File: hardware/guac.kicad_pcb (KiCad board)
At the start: 4 copper layers, 59.5 x 58.5 mm, 72 parts, among them J1 VBUS input fly-leads, J2 Orange TinySLED, J3 Orange TinySLED, J4 AM32 dual ESC, Q1 AO3402, U1 Seeed XIAO RP2350, U10 SK9822-EC20, U11 SN74HC595PWR, U12 SK9822-EC20, U2 AP63205WU-7, U4 LSM6DSV320XTR, U5 H3LIS331DLTR, U6 H3LIS331DLTR, U7 BetaFPV ELRS Lite, U8 SN74AHCT1G125, U9 SN74AHCT1G125

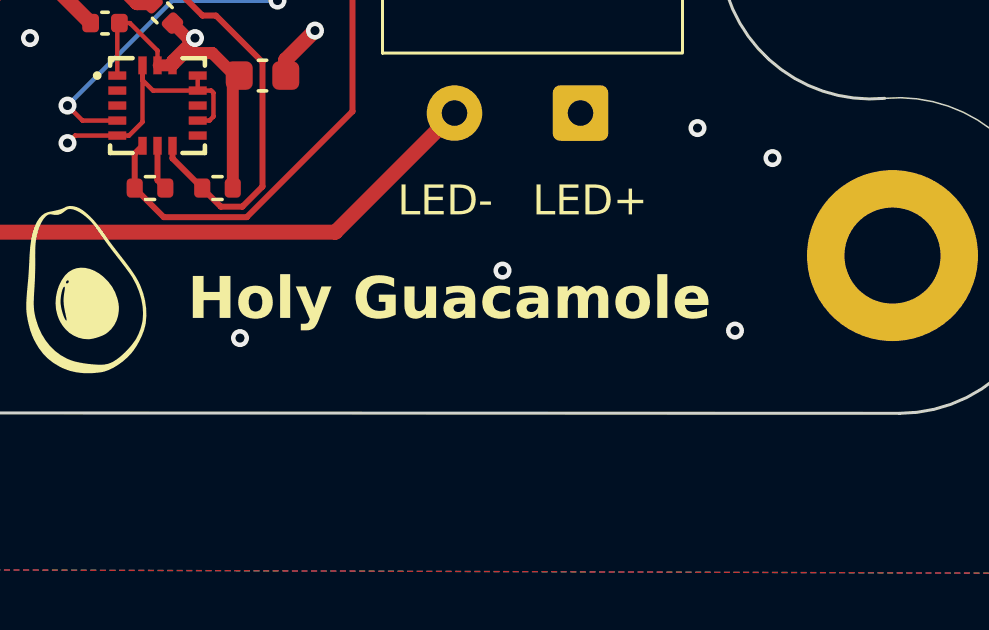
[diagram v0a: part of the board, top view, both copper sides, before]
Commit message: feat: update cad image and silkscreen
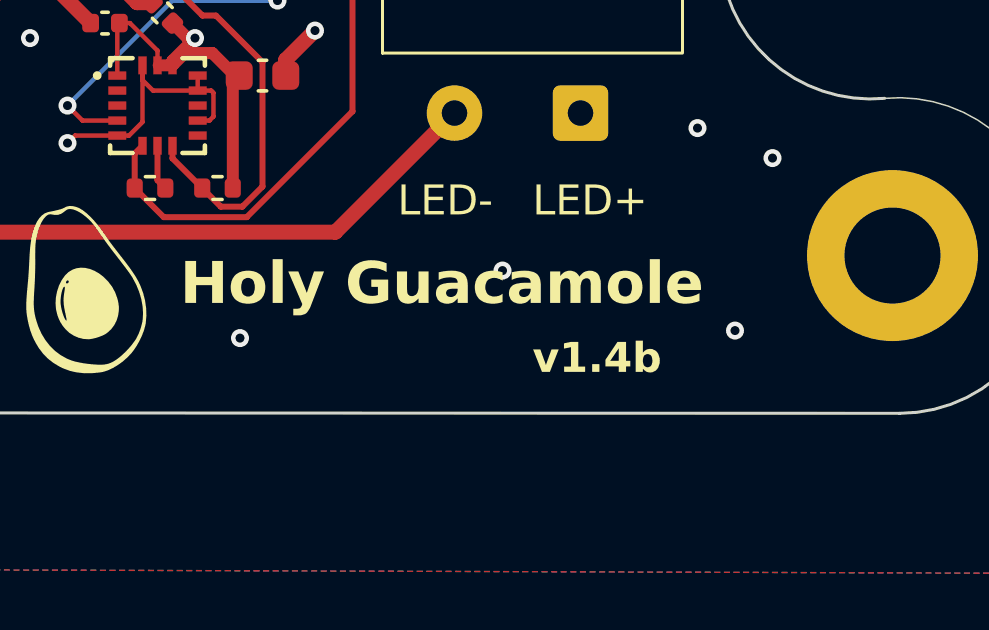
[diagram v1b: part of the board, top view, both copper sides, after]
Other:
- board text added: "v1.4b"
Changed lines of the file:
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@@
 	)
 	(paper "A4")
+	(title_block
+		(title "Holy Guacamole")
+		(date "2026-07-12")
+		(rev "1.4b")
+		(company "Kieran Klukas")
+	)
 	(layers
 		(0 "F.Cu" signal)
@@
 		)
 	)
+	(gr_text "v1.4b"
+		(at 116.25 130.25 0)
+		(layer "F.SilkS")
+		(effects
+			(font
+				(size 1 1)
+				(thickness 0.25)
+				(bold yes)
+			)
+			(justify left bottom)
+		)
+	)
 	(gr_text "Holy Guacamole"
-		(at 104.75 128.5 0)
+		(at 104.5 128 0)
 		(layer "F.SilkS")
 		(effects
@@
 		)
 	)
-	(barcode
-		(at 112.927175 116.177175 0)
-		(layer "B.SilkS")
-		(size 15.85435 15.85435)
-		(text "https://dunkirk.sh")
-		(text_height 1)
-		(type qr)
-		(ecc_level L)
-		(hide yes)
-		(knockout no)
-	)
 	(segment

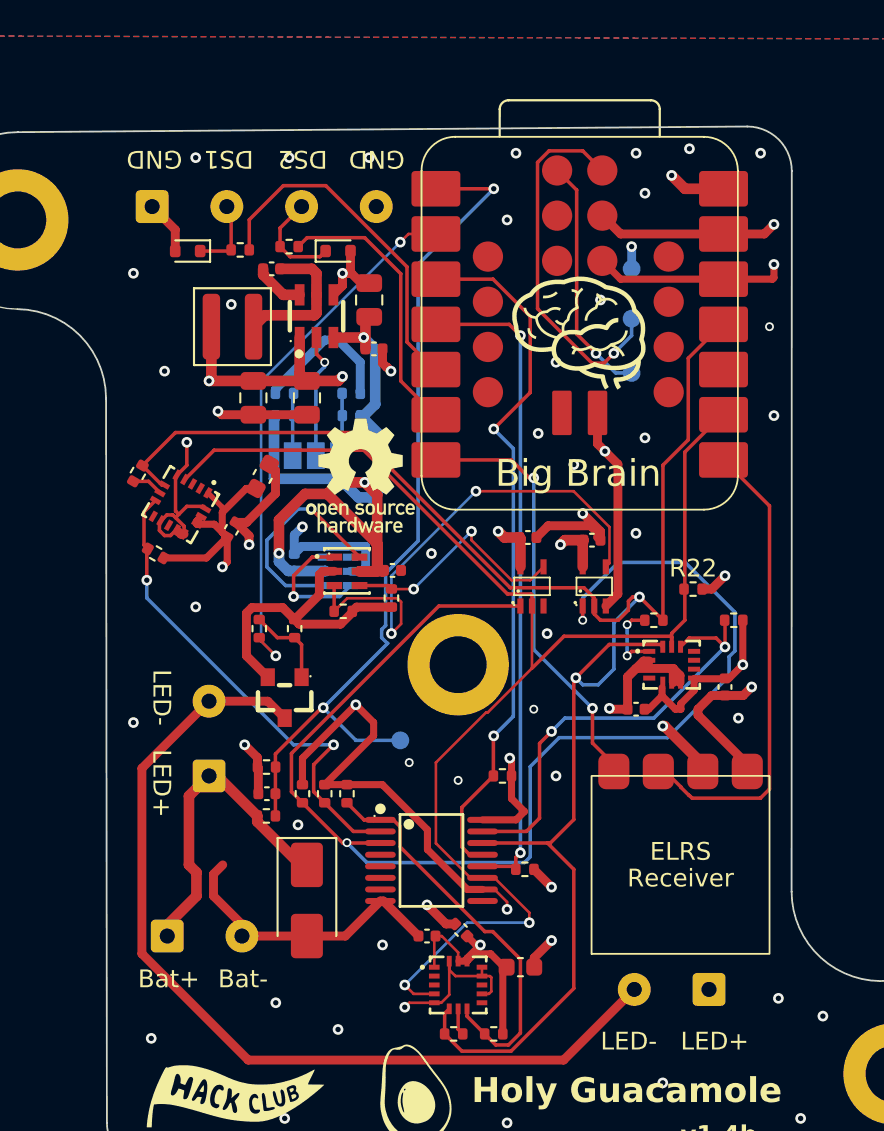
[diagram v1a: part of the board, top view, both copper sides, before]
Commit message: feat: update pcb to use new components
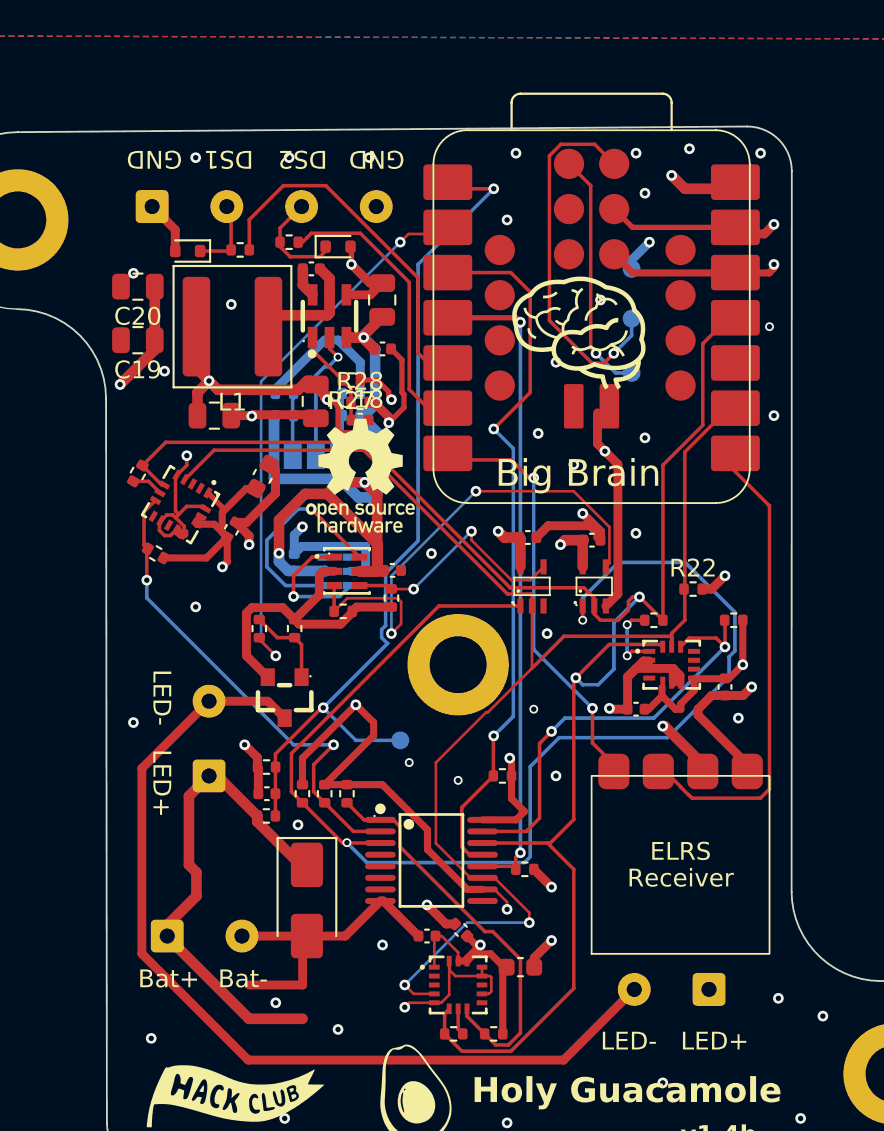
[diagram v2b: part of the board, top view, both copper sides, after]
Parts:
- added C18: 47pf, Capacitor_SMD:C_0402_1005Metric, F.Cu at (98.2, 89.5)
- added C19: 22uf, Capacitor_SMD:C_0805_2012Metric, F.Cu at (85.8, 85.0)
- added C20: 22uf, Capacitor_SMD:C_0805_2012Metric, F.Cu at (85.8, 82.0)
- added R27: 158kΩ, Resistor_SMD:R_0402_1005Metric, F.Cu at (97.8, 87.2)
- added R28: 30.1kΩ, Resistor_SMD:R_0402_1005Metric, F.Cu at (98.2, 88.5)
- L1: value 4.7uH -> 5.6uH; footprint Inductor_SMD:L_Wuerth_MAPI-4020 -> Inductor_SMD:L_Bourns_SRP6060FA
- U2: value AP63205WU-7 -> AP63300WU-7
- moved C5 2.41 mm to (90.0, 89.2), turned to 0 degrees
- moved C3 2.23 mm to (95.5, 81.0)
- moved U1 0.76 mm to (111.2, 83.8)
- moved C1 0.73 mm to (99.5, 82.8)
- moved U2 0.73 mm to (96.5, 83.7)
- moved C4 0.54 mm to (95.8, 88.5)
- moved C2 0.48 mm to (99.5, 85.5)
- moved D4 0.25 mm to (97.0, 79.8)
- moved R13 0.25 mm to (94.2, 79.5)
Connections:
- U2 pad 1: 5V -> /Power Subsystem/BUCK_FB
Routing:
- net VBUS: track 81.5 -> 97.6 mm, vias 1 -> 2
- net 5V: track 62.2 -> 68.6 mm, vias 10 -> 11
- net GND: track 147.3 -> 153.6 mm
- net /Power Subsystem/BUCK_FB: track 0.00 -> 5.55 mm
- net Net-(U2-SW): track 8.23 -> 6.46 mm
- net Net-(U2-BST): track 2.85 -> 1.69 mm
- net 3V3: track 79.8 -> 78.7 mm

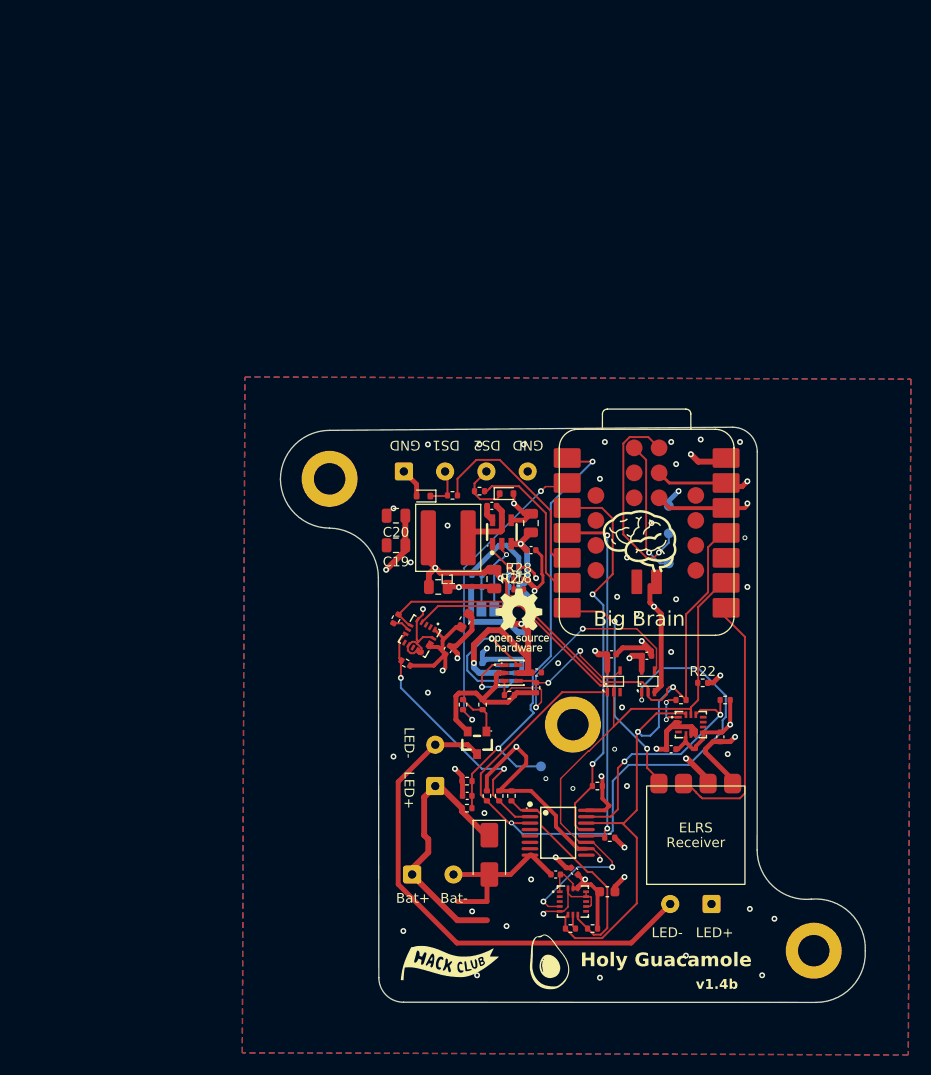
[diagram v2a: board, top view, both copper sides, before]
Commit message: feat: add cern license bit to kicad
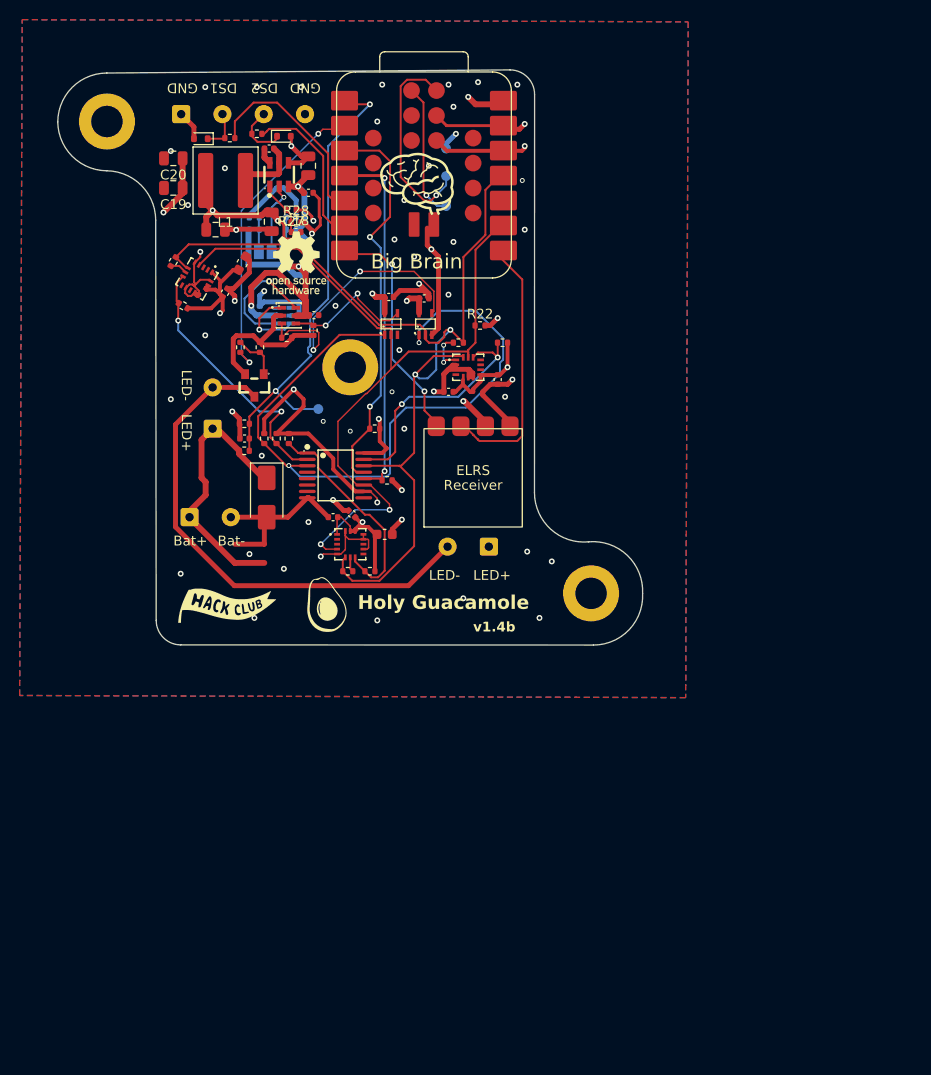
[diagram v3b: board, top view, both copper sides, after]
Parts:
- moved C9 42.8 mm to (81.3, 81.8)
- moved C1 42.8 mm to (76.8, 46.4)
- moved C10 42.8 mm to (68.4, 59.3)
- moved C11 42.8 mm to (96.1, 68.2)
- moved C12 42.8 mm to (70.3, 74.2)
- moved C13 42.8 mm to (84.6, 83.9)
- moved C14 42.8 mm to (85.0, 59.8)
- moved C16 42.8 mm to (77.4, 61.6)
- moved C17 42.8 mm to (71.9, 61.1)
- moved C19 42.8 mm to (63.1, 48.7)
- moved C2 42.8 mm to (76.8, 49.1)
- moved C20 42.8 mm to (63.1, 45.6)
- moved C3 42.8 mm to (72.8, 44.6)
- moved C4 42.8 mm to (73.1, 52.1)
- moved C6 42.8 mm to (70.1, 56.3)
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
